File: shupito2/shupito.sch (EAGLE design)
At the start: 84 parts, among them IC2 74LVC1T45, IC3 74LVC1T45, IC4 74LVC1T45, IC5 74LVC1T45, IC6 ATXMEGA32A4U-AU, IC7 TPS73033DBV, Q1 BC807W-1907646, Q10 1758094, Q11 PDTC123YU-1757992, Q2 NX2301P-1894738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

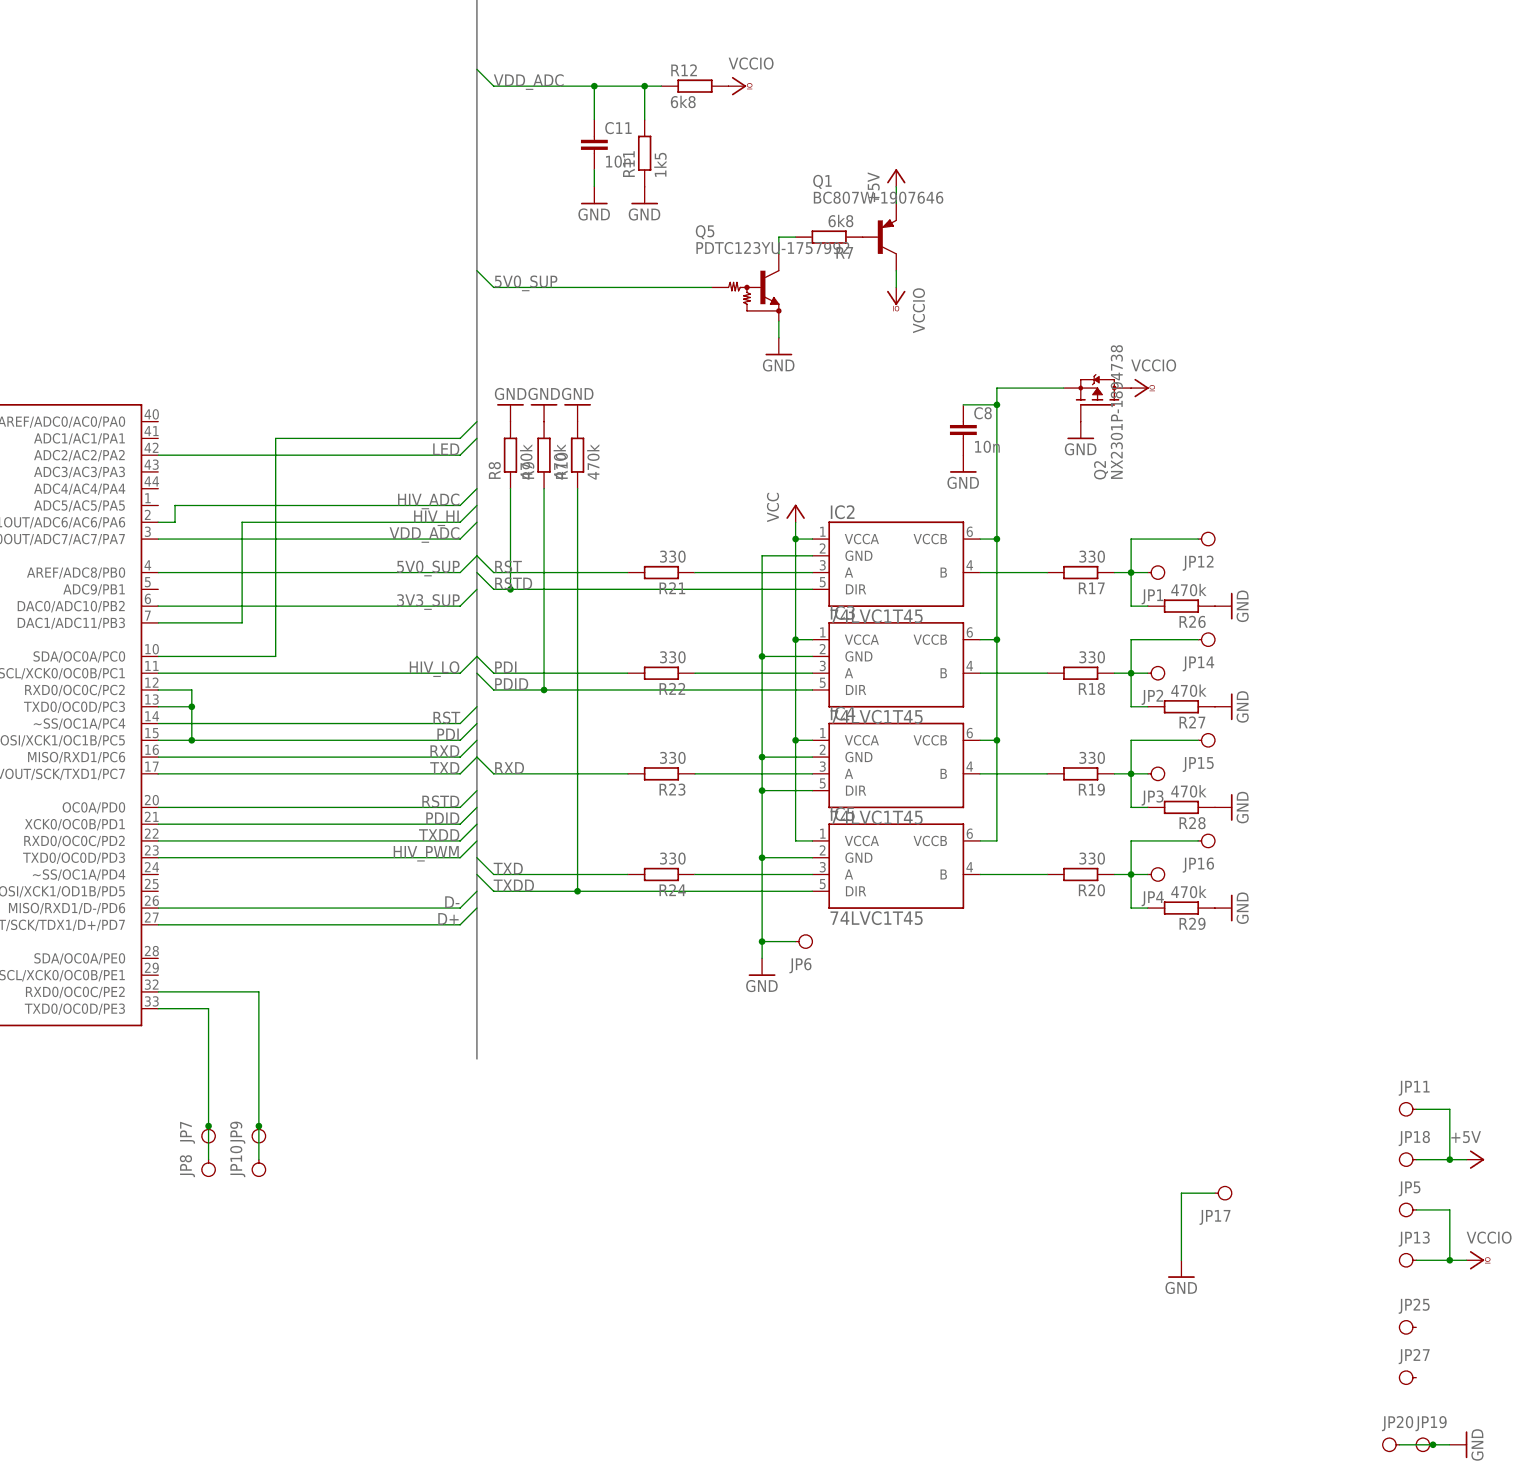
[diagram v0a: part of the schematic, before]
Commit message: Added a button, placement and routing.
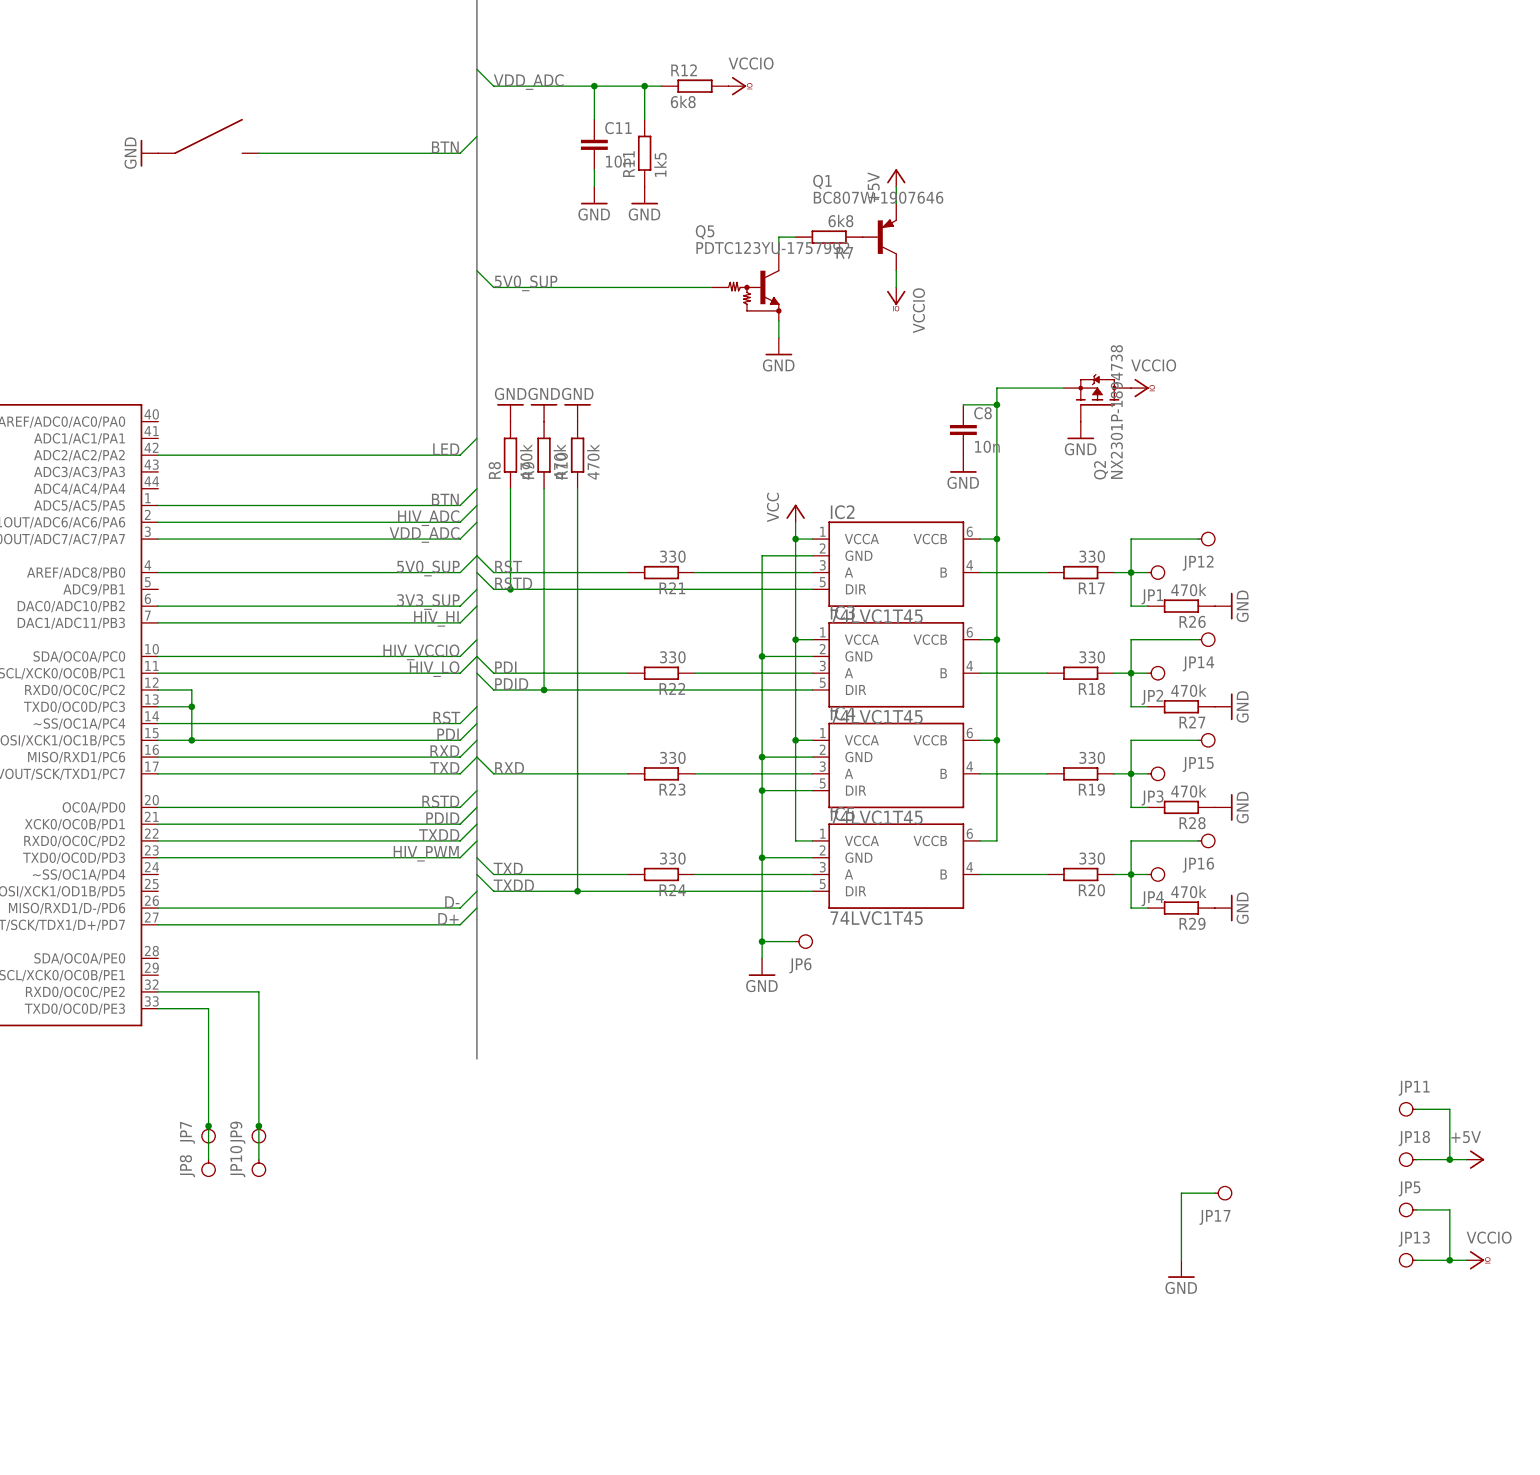
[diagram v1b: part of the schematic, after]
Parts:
- removed JP19, JP20, JP25, JP27: PINH1X01SMD, pinhead_smd:PINH1X01SMD
- added S1: KSS241G, switch:KSS241G
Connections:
- new net BTN: IC6.ADC5/AC5/PA5, S1.P$2
- net GND: now also S1.P$1; no longer JP19.1, JP20.1
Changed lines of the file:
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@@
 <part name="R14" library="rcl" deviceset="R-EU_" device="R0603" value="4k7"/>
 <part name="GND23" library="supply1" deviceset="GND" device=""/>
-<part name="JP25" library="pinhead_smd" deviceset="PINH1X01" device="SMD"/>
-<part name="JP27" library="pinhead_smd" deviceset="PINH1X01" device="SMD"/>
 <part name="IC6" library="xmega" deviceset="ATXMEGA*A4U" device="-AU" technology="32"/>
 <part name="GND5" library="supply1" deviceset="GND" device=""/>
@@
 <part name="C3" library="rcl" deviceset="C-EU" device="C1206" value="4.7u"/>
 <part name="GND7" library="supply1" deviceset="GND" device=""/>
-<part name="JP19" library="pinhead_smd" deviceset="PINH1X01" device="SMD"/>
-<part name="JP20" library="pinhead_smd" deviceset="PINH1X01" device="SMD"/>
+<part name="S1" library="switch" deviceset="KSS" device="G" technology="241"/>
 <part name="GND8" library="supply1" deviceset="GND" device=""/>
 </parts>
@@
 <instance part="R14" gate="G$1" x="119.38" y="325.12" rot="R270"/>
 <instance part="GND23" gate="1" x="119.38" y="332.74" rot="MR180"/>
-<instance part="JP25" gate="G$1" x="287.02" y="-15.24"/>
-<instance part="JP27" gate="G$1" x="287.02" y="-22.86"/>
 <instance part="IC6" gate="G$1" x="66.04" y="78.74"/>
 <instance part="GND5" gate="1" x="27.94" y="66.04"/>
@@
 <instance part="C3" gate="G$1" x="114.3" y="294.64"/>
 <instance part="GND7" gate="1" x="114.3" y="279.4" rot="MR0"/>
-<instance part="JP19" gate="G$1" x="289.56" y="-33.02"/>
-<instance part="JP20" gate="G$1" x="284.48" y="-33.02"/>
-<instance part="GND8" gate="1" x="297.18" y="-33.02" rot="R90"/>
+<instance part="S1" gate="G$1" x="106.68" y="162.56"/>
+<instance part="GND8" gate="1" x="96.52" y="162.56" rot="R270"/>
 </instances>
 <busses>
-<bus name="RST,PDI,RXD,TXD,RSTD,PDID,TXDD,USB_RX,USB_TX,5V0_SUP,3V3_SUP,VDD_ADC,SYS_CLK,USB_XCK,PWR_EN,USB_VCC,D+,D-,USB_PDI,USB_PDO,USB_SCK,USB_RX,USB_TX,SYS_CLK,USB_XCK,LED,PWR_EN,SWITCHED_5V,EM_BOOT,USB_CTS,USB_RTR,SYS_CLK,HIV_ADC,HIV_PWM,HIV_HI,HIV_LO,HIV_VCCIO">
+<bus name="RST,PDI,RXD,TXD,RSTD,PDID,TXDD,USB_RX,USB_TX,5V0_SUP,3V3_SUP,VDD_ADC,SYS_CLK,USB_XCK,PWR_EN,USB_VCC,D+,D-,USB_PDI,USB_PDO,USB_SCK,USB_RX,USB_TX,SYS_CLK,USB_XCK,LED,PWR_EN,SWITCHED_5V,EM_BOOT,USB_CTS,USB_RTR,SYS_CLK,HIV_ADC,HIV_PWM,HIV_HI,HIV_LO,HIV_VCCIO,BTN">
 <segment>
 <wire x1="147.32" y1="332.74" x2="147.32" y2="25.4" width="0.762" layer="92"/>
@@
 </segment>
 <segment>
-<pinref part="JP20" gate="G$1" pin="1"/>
-<pinref part="JP19" gate="G$1" pin="1"/>
-<wire x1="287.02" y1="-33.02" x2="292.1" y2="-33.02" width="0.1524" layer="91"/>
-<wire x1="292.1" y1="-33.02" x2="294.64" y2="-33.02" width="0.1524" layer="91"/>
+<pinref part="S1" gate="G$1" pin="P$1"/>
 <pinref part="GND8" gate="1" pin="GND"/>
-<junction x="292.1" y="-33.02"/>
 </segment>
 </net>
@@
 </segment>
 <segment>
-<wire x1="144.78" y1="109.22" x2="147.32" y2="111.76" width="0.1524" layer="91"/>
-<label x="144.78" y="109.22" size="1.778" layer="95" rot="MR0"/>
-<wire x1="144.78" y1="109.22" x2="101.6" y2="109.22" width="0.1524" layer="91"/>
-<wire x1="101.6" y1="109.22" x2="101.6" y2="106.68" width="0.1524" layer="91"/>
+<wire x1="144.78" y1="106.68" x2="147.32" y2="109.22" width="0.1524" layer="91"/>
+<label x="144.78" y="106.68" size="1.778" layer="95" rot="MR0"/>
+<wire x1="144.78" y1="106.68" x2="99.06" y2="106.68" width="0.1524" layer="91"/>
 <pinref part="IC6" gate="G$1" pin="AC1OUT/ADC6/AC6/PA6"/>
-<wire x1="101.6" y1="106.68" x2="99.06" y2="106.68" width="0.1524" layer="91"/>
 </segment>
 </net>
@@
 </segment>
 <segment>
-<wire x1="111.76" y1="106.68" x2="144.78" y2="106.68" width="0.1524" layer="91"/>
-<wire x1="144.78" y1="106.68" x2="147.32" y2="109.22" width="0.1524" layer="91"/>
-<label x="144.78" y="106.68" size="1.778" layer="95" rot="MR0"/>
-<wire x1="111.76" y1="106.68" x2="111.76" y2="91.44" width="0.1524" layer="91"/>
+<wire x1="99.06" y1="91.44" x2="144.78" y2="91.44" width="0.1524" layer="91"/>
+<wire x1="144.78" y1="91.44" x2="147.32" y2="93.98" width="0.1524" layer="91"/>
+<label x="144.78" y="91.44" size="1.778" layer="95" rot="MR0"/>
 <pinref part="IC6" gate="G$1" pin="DAC1/ADC11/PB3"/>
-<wire x1="99.06" y1="91.44" x2="111.76" y2="91.44" width="0.1524" layer="91"/>
 </segment>
 </net>
@@
 </segment>
 <segment>
-<wire x1="116.84" y1="119.38" x2="144.78" y2="119.38" width="0.1524" layer="91"/>
-<wire x1="144.78" y1="119.38" x2="147.32" y2="121.92" width="0.1524" layer="91"/>
+<wire x1="99.06" y1="86.36" x2="144.78" y2="86.36" width="0.1524" layer="91"/>
+<wire x1="144.78" y1="86.36" x2="147.32" y2="88.9" width="0.1524" layer="91"/>
 <pinref part="IC6" gate="G$1" pin="SDA/OC0A/PC0"/>
-<wire x1="116.84" y1="119.38" x2="116.84" y2="86.36" width="0.1524" layer="91"/>
-<wire x1="116.84" y1="86.36" x2="99.06" y2="86.36" width="0.1524" layer="91"/>
+<label x="144.78" y="86.36" size="1.778" layer="95" rot="MR0"/>
 </segment>
 </net>
@@
 </segment>
 </net>
+<net name="BTN" class="0">
+<segment>
+<pinref part="S1" gate="G$1" pin="P$2"/>
+<wire x1="114.3" y1="162.56" x2="144.78" y2="162.56" width="0.1524" layer="91"/>
+<wire x1="144.78" y1="162.56" x2="147.32" y2="165.1" width="0.1524" layer="91"/>
+<label x="144.78" y="162.56" size="1.778" layer="95" rot="MR0"/>
+</segment>
+<segment>
+<pinref part="IC6" gate="G$1" pin="ADC5/AC5/PA5"/>
+<wire x1="99.06" y1="109.22" x2="144.78" y2="109.22" width="0.1524" layer="91"/>
+<wire x1="144.78" y1="109.22" x2="147.32" y2="111.76" width="0.1524" layer="91"/>
+<label x="144.78" y="109.22" size="1.778" layer="95" rot="MR0"/>
+</segment>
+</net>

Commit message: Routed.
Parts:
- added JP19, JP20: PINH1X01SMD, pinhead_smd:PINH1X01SMD
- added R3, R4: 0, rcl:R-EU_R1206
- added TP3, TP4, TP5: TPTP15SQ, testpad:TPTP15SQ
- C1, C11, C4, C5, C8: device rcl:C-EUC0603 -> rcl:C-EUC0603K
- C13: value 4.7u -> 1u/25V-1759039; device rcl:C-EUC0603 -> rcl:C-EUC0603K
- C2: value 100n -> 10n; device rcl:C-EUC0603 -> rcl:C-EUC0603K
- C3: value 4.7u -> 2.2u-1759473; device rcl:C-EUC1206 -> rcl:C-EUC0603K
- C6: device rcl:C-EUC1206 -> rcl:C-EUC0603K
- C7: value 4.7u -> 2.2u; device rcl:C-EUC1206 -> rcl:C-EUC0603K
- L2: value (none) -> 10uH-1463501; device rcl:R-US_R0603 -> rcl:R-US_R0805
- Q6, Q9: value (none) -> DTA144-1680214
- R11: value 1k5 -> 1k5 1%
- R12, R30, R7: value 6k8 -> 6k8 1%
- R13: value 4k7 -> 15k 1%
- R14: value 4k7 -> 1k 1%
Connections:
- new net GND2: C13.2, C3.2, Q10.S, R2.2, R3.2
- new net N$11: Q9.E, R4.2
- net GND: now also JP19.1, JP20.1, R3.1; no longer C13.2, C3.2, Q10.S, R2.2
- net HIV_ADC: now also IC6.ADC1/AC1/PA1; no longer IC6.AC1OUT/ADC6/AC6/PA6
- net HIV_LO: now also IC6.SDA/OC0A/PC0; no longer IC6.SCL/XCK0/OC0B/PC1
- net HIV_VCCIO: now also IC6.~SS/OC1A/PC4; no longer IC6.SDA/OC0A/PC0
- net LED: now also IC6.ADC3/AC3/PA3; no longer IC6.ADC2/AC2/PA2
- net N$22: now also R4.1, TP3.TP; no longer Q9.E
- net RST: now also IC6.SCL/XCK0/OC0B/PC1; no longer IC6.~SS/OC1A/PC4
- net VCC: now also TP4.TP, TP5.TP
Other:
- moved on the sheet: JP10, JP11, JP13, JP17, JP18, JP5, JP7, JP8, JP9, R13, R14

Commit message: Done.
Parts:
- L2: value 10uH-1463501 -> 10uH-1463501, 22uH-1612131
- R13: value 15k 1% -> 22k 1%
- R14: value 1k 1% -> 1k5 1%
- R2: value 4k7 -> 6k8
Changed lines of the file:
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@@
 <part name="Q7" library="transistors" deviceset="NPN-BIAS" device="-SOT323-BEC" value="PDTC123YU-1757992"/>
 <part name="Q8" library="transistors" deviceset="NPN-BIAS" device="-SOT323-BEC" value="PDTC123YU-1757992"/>
-<part name="L2" library="rcl" deviceset="R-US_" device="R0805" value="10uH-1463501"/>
+<part name="L2" library="rcl" deviceset="R-US_" device="R0805" value="10uH-1463501, 22uH-1612131"/>
 <part name="C13" library="rcl" deviceset="C-EU" device="C0603K" value="1u/25V-1759039"/>
 <part name="D2" library="diode" deviceset="DIODE" device="-SOD323" value="BAT42WS-1621831"/>
 <part name="Q10" library="transistors" deviceset="N-MOSFET" device="-SOT323-GSD" value="1758094"/>
 <part name="R1" library="rcl" deviceset="R-EU_" device="R0603" value="330"/>
-<part name="R2" library="rcl" deviceset="R-EU_" device="R0603" value="4k7"/>
+<part name="R2" library="rcl" deviceset="R-EU_" device="R0603" value="6k8"/>
 <part name="Q9" library="transistors" deviceset="PNP-BIAS" device="-SOT323-BEC" value="DTA144-1680214"/>
-<part name="R13" library="rcl" deviceset="R-EU_" device="R0603" value="15k 1%"/>
-<part name="R14" library="rcl" deviceset="R-EU_" device="R0603" value="1k 1%"/>
+<part name="R13" library="rcl" deviceset="R-EU_" device="R0603" value="22k 1%"/>
+<part name="R14" library="rcl" deviceset="R-EU_" device="R0603" value="1k5 1%"/>
 <part name="GND23" library="supply1" deviceset="GND" device=""/>
 <part name="IC6" library="xmega" deviceset="ATXMEGA*A4U" device="-AU" technology="32"/>
